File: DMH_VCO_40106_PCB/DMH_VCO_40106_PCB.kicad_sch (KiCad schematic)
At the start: 0 parts

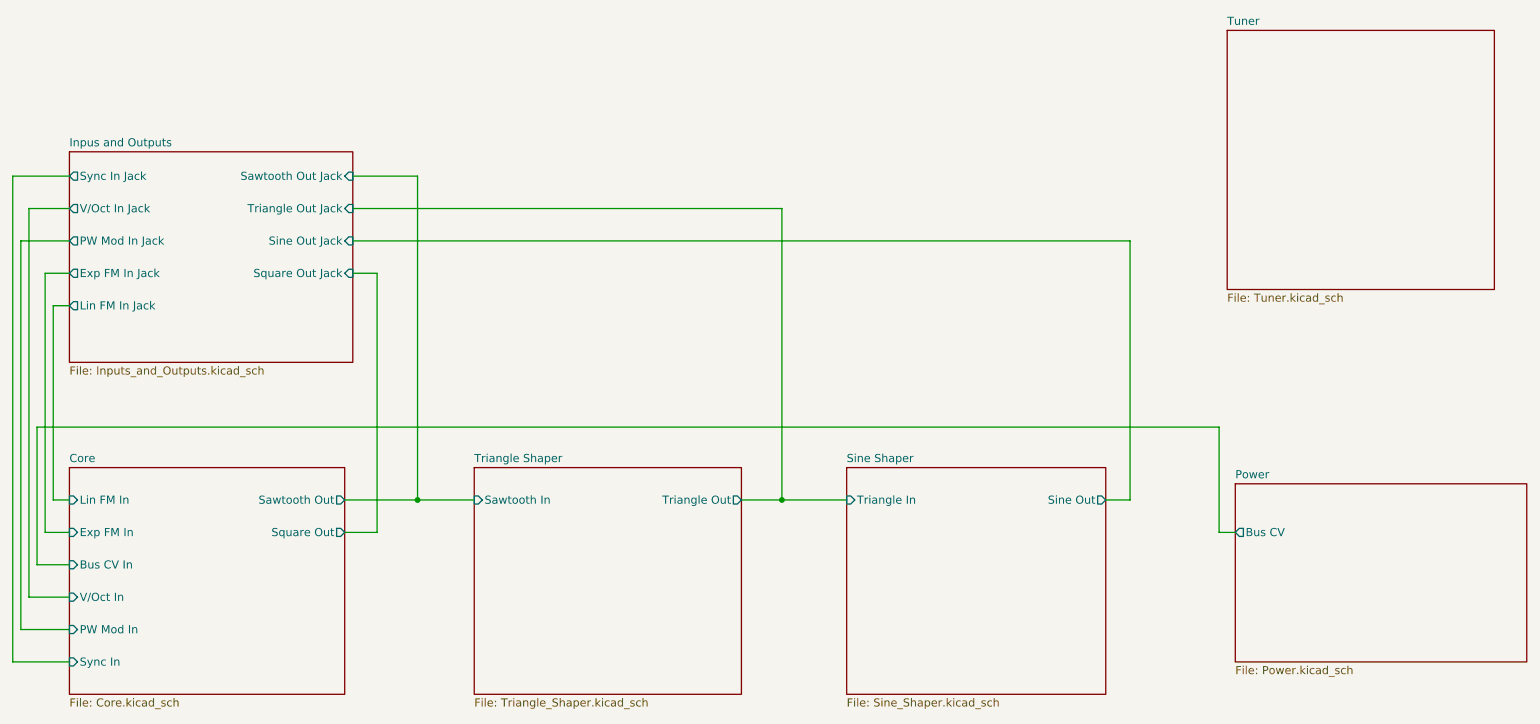
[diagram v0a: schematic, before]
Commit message: Updates from testing on breadboard
- Removed Bus CV input, normalled it to V/oct input jack instead
- Renamed Lin FM input to Exp FM In 2
- Added annotations about temporary resistor/pot values
- Added annotations about pots and trimpots pinout
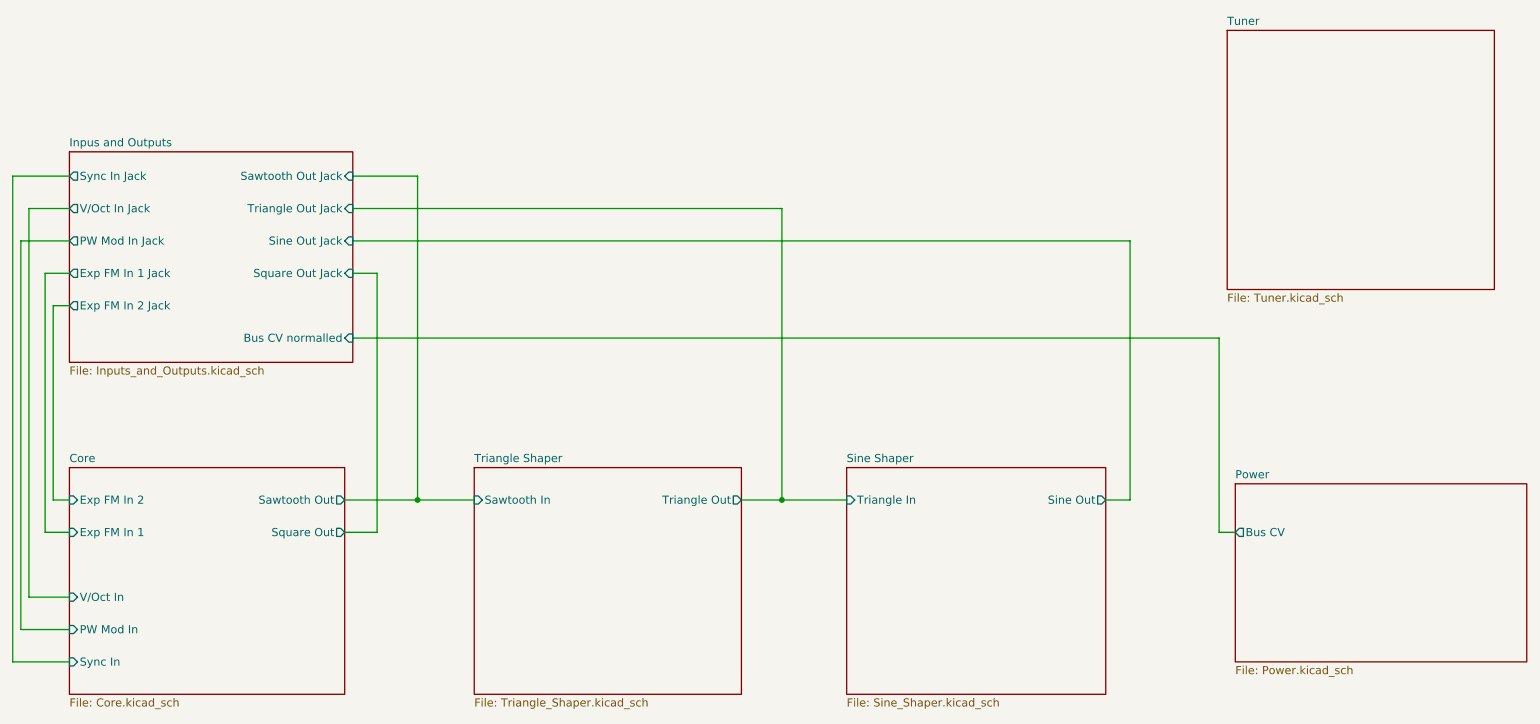
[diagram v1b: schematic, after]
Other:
- sheet Core ports: added Exp FM In 1, Exp FM In 2; removed Bus CV In, Exp FM In, Lin FM In
- sheet Inpus and Outputs ports: added Bus CV normalled, Exp FM In 1 Jack, Exp FM In 2 Jack; removed Exp FM In Jack, Lin FM In Jack
- company: DMH -> DMH Instruments
- title: VCO mki PCB -> VCO 40106 PCB
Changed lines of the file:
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@@
 	(paper "A4")
 	(title_block
-		(title "VCO mki PCB")
+		(title "VCO 40106 PCB")
 		(date "2024-06-16")
 		(rev "1")
-		(company "DMH")
+		(company "DMH Instruments")
 	)
 	(junction
@@
 	(wire
 		(pts
-			(xy 22.86 114.3) (xy 22.86 92.71)
-		)
-		(stroke
-			(width 0)
-			(type default)
-		)
-	)
-	(wire
-		(pts
 			(xy 20.32 63.5) (xy 27.94 63.5)
 		)
@@
 	(wire
 		(pts
-			(xy 208.28 92.71) (xy 208.28 109.22)
-		)
-		(stroke
-			(width 0)
-			(type default)
-		)
-	)
-	(wire
-		(pts
 			(xy 27.94 124.46) (xy 20.32 124.46)
 		)
@@
 	(wire
 		(pts
+			(xy 208.28 78.74) (xy 208.28 109.22)
+		)
+		(stroke
+			(width 0)
+			(type default)
+		)
+	)
+	(wire
+		(pts
 			(xy 19.05 129.54) (xy 27.94 129.54)
 		)
@@
 	(wire
 		(pts
-			(xy 22.86 92.71) (xy 208.28 92.71)
-		)
-		(stroke
-			(width 0)
-			(type default)
-		)
-	)
-	(wire
-		(pts
 			(xy 27.94 68.58) (xy 24.13 68.58)
 		)
@@
 	(wire
 		(pts
+			(xy 208.28 78.74) (xy 72.39 78.74)
+		)
+		(stroke
+			(width 0)
+			(type default)
+		)
+	)
+	(wire
+		(pts
 			(xy 24.13 68.58) (xy 24.13 109.22)
 		)
@@
 		(pts
 			(xy 27.94 119.38) (xy 21.59 119.38)
-		)
-		(stroke
-			(width 0)
-			(type default)
-		)
-	)
-	(wire
-		(pts
-			(xy 27.94 114.3) (xy 22.86 114.3)
 		)
 		(stroke
@@
 			)
 		)
-		(pin "Lin FM In" input
+		(pin "Exp FM In 2" input
 			(at 27.94 104.14 180)
 			(effects
@@
 			)
 		)
-		(pin "Exp FM In" input
+		(pin "Exp FM In 1" input
 			(at 27.94 109.22 180)
-			(effects
-				(font
-					(size 1.27 1.27)
-				)
-				(justify left)
-			)
-		)
-		(pin "Bus CV In" input
-			(at 27.94 114.3 180)
 			(effects
 				(font
@@
 			)
 		)
-		(pin "Exp FM In Jack" output
+		(pin "Exp FM In 1 Jack" output
 			(at 27.94 68.58 180)
 			(effects
@@
 			)
 		)
-		(pin "Lin FM In Jack" output
+		(pin "Exp FM In 2 Jack" output
 			(at 27.94 73.66 180)
 			(effects
@@
 			(effects
 				(font
+					(size 1.27 1.27)
+				)
+				(justify right)
+			)
+		)
+		(pin "Bus CV normalled" input
+			(at 72.39 78.74 0)
+			(effects
+				(font

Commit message: Adjusted all output gains to 10Vpp
... and added buffer stages for Sawtooth Out and Triangle Out in order to avoid modifying Triangle and Sine wafeform characteristics when connecting Sawtooth Out and Triangle Out to other modules.
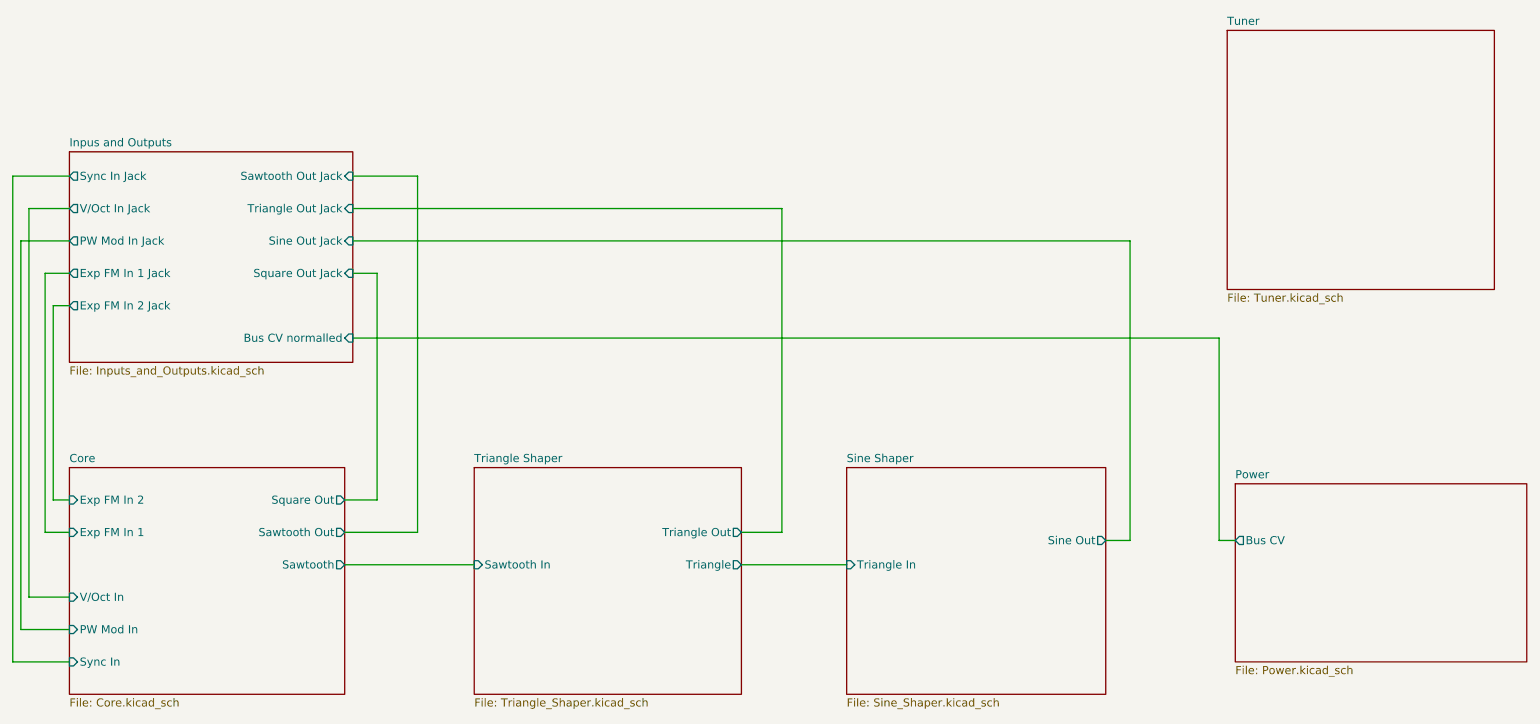
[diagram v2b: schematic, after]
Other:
- sheet Core ports: added Sawtooth; removed none
- sheet Triangle Shaper ports: added Triangle; removed none
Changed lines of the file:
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@@
 		(company "DMH Instruments")
 	)
-	(junction
-		(at 139.7 104.14)
-		(diameter 0)
-		(color 0 0 0 0)
-	)
-	(junction
-		(at 82.55 104.14)
-		(diameter 0)
-		(color 0 0 0 0)
-	)
 	(wire
 		(pts
@@
 	(wire
 		(pts
-			(xy 208.28 109.22) (xy 210.82 109.22)
-		)
-		(stroke
-			(width 0)
-			(type default)
-		)
-	)
-	(wire
-		(pts
-			(xy 194.31 104.14) (xy 194.31 63.5)
+			(xy 208.28 110.49) (xy 210.82 110.49)
+		)
+		(stroke
+			(width 0)
+			(type default)
+		)
+	)
+	(wire
+		(pts
+			(xy 194.31 110.49) (xy 194.31 63.5)
 		)
 		(stroke
@@
 	(wire
 		(pts
-			(xy 71.12 109.22) (xy 76.2 109.22)
-		)
-		(stroke
-			(width 0)
-			(type default)
-		)
-	)
-	(wire
-		(pts
-			(xy 139.7 58.42) (xy 139.7 104.14)
-		)
-		(stroke
-			(width 0)
-			(type default)
-		)
-	)
-	(wire
-		(pts
-			(xy 139.7 104.14) (xy 133.35 104.14)
-		)
-		(stroke
-			(width 0)
-			(type default)
-		)
-	)
-	(wire
-		(pts
-			(xy 208.28 78.74) (xy 208.28 109.22)
+			(xy 71.12 104.14) (xy 76.2 104.14)
+		)
+		(stroke
+			(width 0)
+			(type default)
+		)
+	)
+	(wire
+		(pts
+			(xy 139.7 109.22) (xy 133.35 109.22)
+		)
+		(stroke
+			(width 0)
+			(type default)
+		)
+	)
+	(wire
+		(pts
+			(xy 208.28 78.74) (xy 208.28 110.49)
 		)
 		(stroke
@@
 	(wire
 		(pts
-			(xy 71.12 104.14) (xy 82.55 104.14)
+			(xy 71.12 109.22) (xy 82.55 109.22)
 		)
 		(stroke
@@
 	(wire
 		(pts
-			(xy 139.7 104.14) (xy 149.86 104.14)
-		)
-		(stroke
-			(width 0)
-			(type default)
-		)
-	)
-	(wire
-		(pts
-			(xy 82.55 104.14) (xy 91.44 104.14)
-		)
-		(stroke
-			(width 0)
-			(type default)
-		)
-	)
-	(wire
-		(pts
 			(xy 82.55 53.34) (xy 72.39 53.34)
 		)
@@
 	(wire
 		(pts
+			(xy 71.12 114.3) (xy 91.44 114.3)
+		)
+		(stroke
+			(width 0)
+			(type default)
+		)
+	)
+	(wire
+		(pts
 			(xy 24.13 68.58) (xy 24.13 109.22)
 		)
@@
 	(wire
 		(pts
-			(xy 76.2 109.22) (xy 76.2 68.58)
-		)
-		(stroke
-			(width 0)
-			(type default)
-		)
-	)
-	(wire
-		(pts
-			(xy 82.55 104.14) (xy 82.55 53.34)
+			(xy 76.2 104.14) (xy 76.2 68.58)
+		)
+		(stroke
+			(width 0)
+			(type default)
+		)
+	)
+	(wire
+		(pts
+			(xy 139.7 58.42) (xy 139.7 109.22)
+		)
+		(stroke
+			(width 0)
+			(type default)
+		)
+	)
+	(wire
+		(pts
+			(xy 82.55 109.22) (xy 82.55 53.34)
 		)
 		(stroke
@@
 	(wire
 		(pts
-			(xy 190.5 104.14) (xy 194.31 104.14)
+			(xy 133.35 114.3) (xy 149.86 114.3)
+		)
+		(stroke
+			(width 0)
+			(type default)
+		)
+	)
+	(wire
+		(pts
+			(xy 190.5 110.49) (xy 194.31 110.49)
 		)
 		(stroke
@@
 		)
 		(pin "Triangle Out" output
-			(at 133.35 104.14 0)
+			(at 133.35 109.22 0)
 			(effects
 				(font
@@
 		)
 		(pin "Sawtooth In" input
-			(at 91.44 104.14 180)
-			(effects
-				(font
-					(size 1.27 1.27)
-				)
-				(justify left)
+			(at 91.44 114.3 180)
+			(effects
+				(font
+					(size 1.27 1.27)
+				)
+				(justify left)
+			)
+		)
+		(pin "Triangle" output
+			(at 133.35 114.3 0)
+			(effects
+				(font
+					(size 1.27 1.27)
+				)
+				(justify right)
 			)
 		)
@@
 		)
 		(pin "Sine Out" output
-			(at 190.5 104.14 0)
+			(at 190.5 110.49 0)
 			(effects
 				(font
@@
 		)
 		(pin "Triangle In" input
-			(at 149.86 104.14 180)
+			(at 149.86 114.3 180)
 			(effects
 				(font
@@
 		)
 		(pin "Sawtooth Out" output
+			(at 71.12 109.22 0)
+			(effects
+				(font
+					(size 1.27 1.27)
+				)
+				(justify right)
+			)
+		)
+		(pin "Square Out" output
 			(at 71.12 104.14 0)
-			(effects
-				(font
-					(size 1.27 1.27)
-				)
-				(justify right)
-			)
-		)
-		(pin "Square Out" output
-			(at 71.12 109.22 0)
 			(effects
 				(font
@@
 				)
 				(justify left)
+			)
+		)
+		(pin "Sawtooth" output
+			(at 71.12 114.3 0)
+			(effects
+				(font
+					(size 1.27 1.27)
+				)
+				(justify right)
 			)
 		)
@@
 		)
 		(pin "Bus CV" output
-			(at 210.82 109.22 180)
-			(effects
-				(font
+			(at 210.82 110.49 180)
+			(effects
+				(font

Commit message: Added tuner circuit
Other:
- sheet Tuner ports: added Sawtooth In; removed none
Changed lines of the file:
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@@
 		(company "DMH Instruments")
 	)
+	(junction
+		(at 86.36 114.3)
+		(diameter 0)
+		(color 0 0 0 0)
+	)
 	(wire
 		(pts
@@
 	(wire
 		(pts
+			(xy 209.55 53.34) (xy 86.36 53.34)
+		)
+		(stroke
+			(width 0)
+			(type default)
+		)
+	)
+	(wire
+		(pts
 			(xy 139.7 109.22) (xy 133.35 109.22)
 		)
@@
 	(wire
 		(pts
+			(xy 86.36 53.34) (xy 86.36 114.3)
+		)
+		(stroke
+			(width 0)
+			(type default)
+		)
+	)
+	(wire
+		(pts
 			(xy 27.94 68.58) (xy 24.13 68.58)
 		)
@@
 	(wire
 		(pts
-			(xy 71.12 109.22) (xy 82.55 109.22)
+			(xy 71.12 109.22) (xy 81.28 109.22)
 		)
 		(stroke
@@
 	(wire
 		(pts
-			(xy 82.55 53.34) (xy 72.39 53.34)
+			(xy 81.28 53.34) (xy 72.39 53.34)
 		)
 		(stroke
@@
 	(wire
 		(pts
-			(xy 71.12 114.3) (xy 91.44 114.3)
+			(xy 71.12 114.3) (xy 86.36 114.3)
 		)
 		(stroke
@@
 	(wire
 		(pts
+			(xy 86.36 114.3) (xy 91.44 114.3)
+		)
+		(stroke
+			(width 0)
+			(type default)
+		)
+	)
+	(wire
+		(pts
 			(xy 76.2 104.14) (xy 76.2 68.58)
 		)
@@
 	(wire
 		(pts
-			(xy 82.55 109.22) (xy 82.55 53.34)
+			(xy 81.28 109.22) (xy 81.28 53.34)
 		)
 		(stroke
@@
 			)
 		)
+		(pin "Sawtooth In" input
+			(at 209.55 53.34 180)
+			(effects
+				(font
+					(size 1.27 1.27)
+				)
+				(justify left)
+			)
+		)

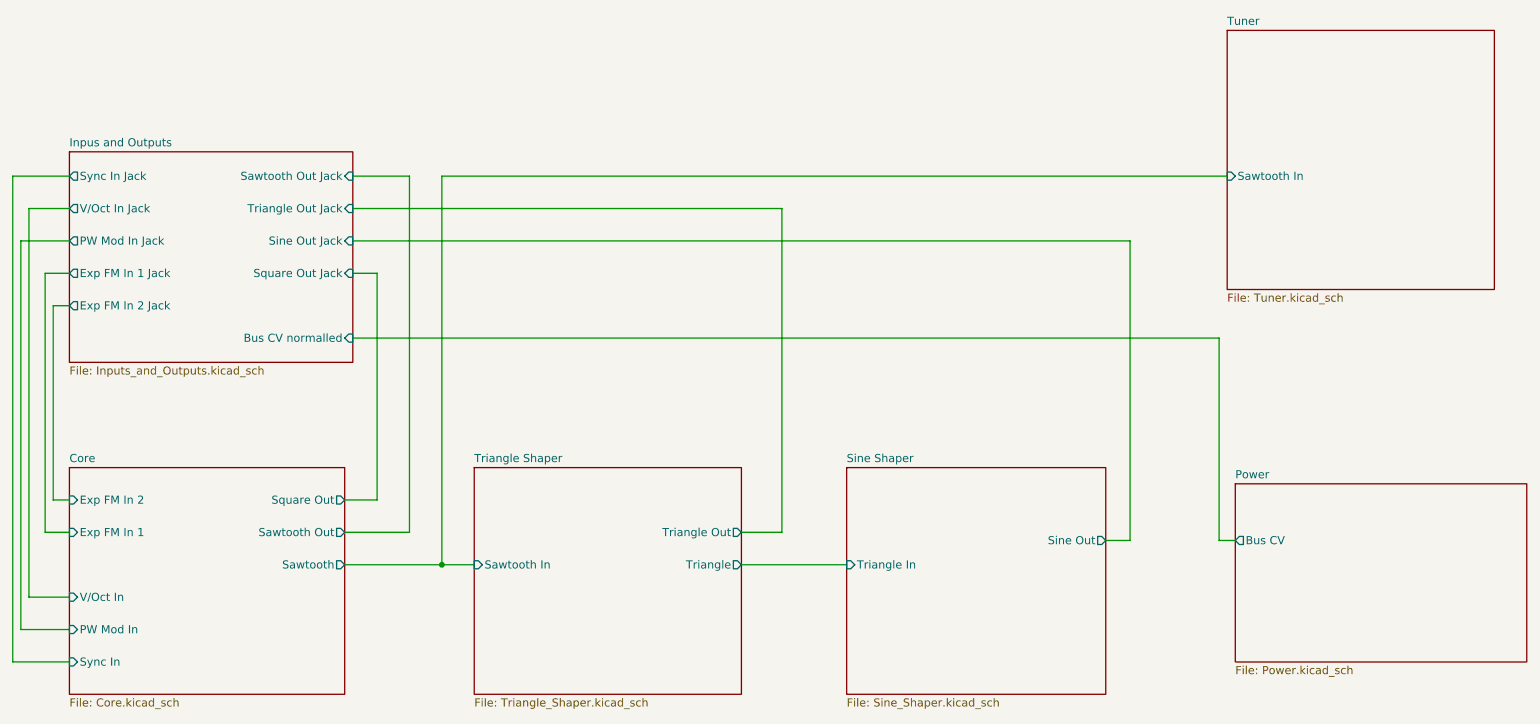
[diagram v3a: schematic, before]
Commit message: Prepared Inputs/Outputs sheet to split in 2 PCBs
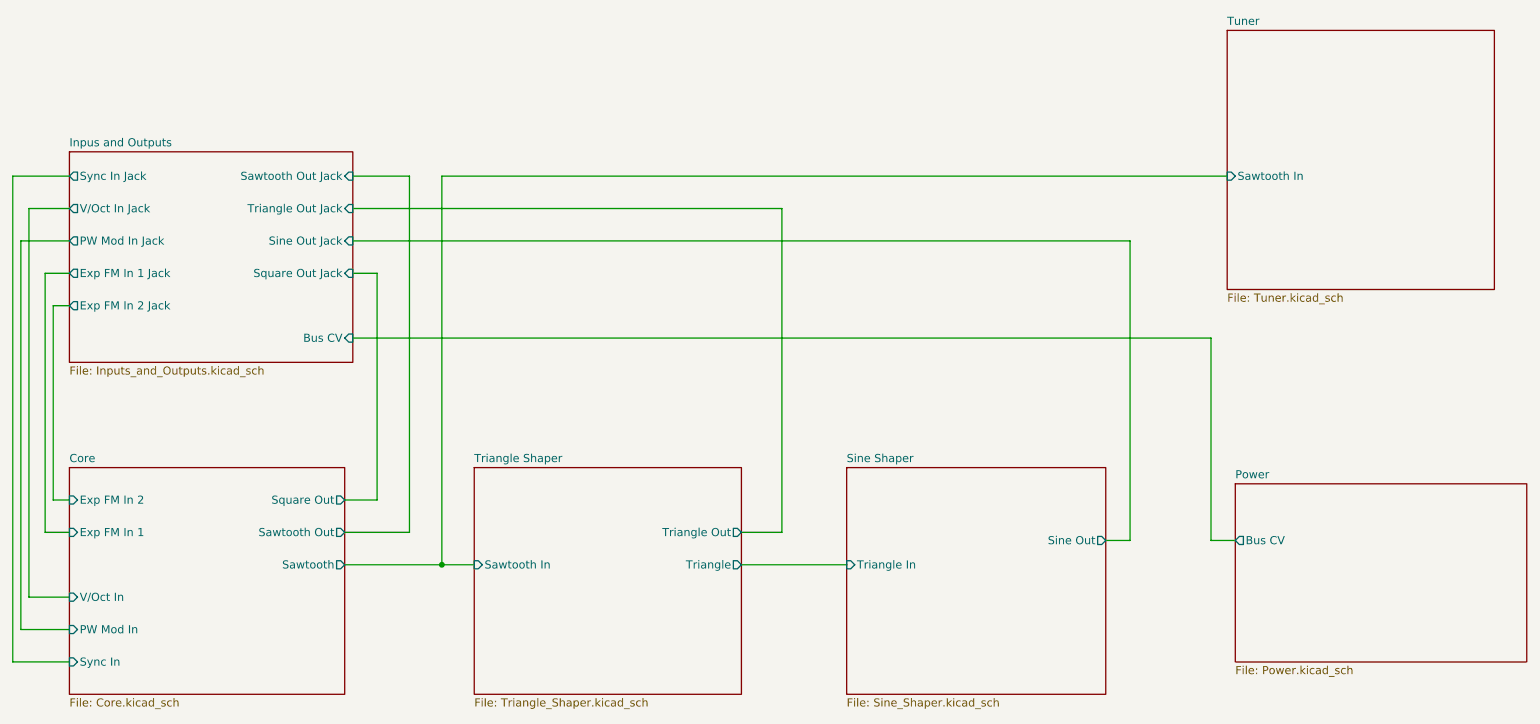
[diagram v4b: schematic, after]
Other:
- sheet Inpus and Outputs ports: added Bus CV; removed Bus CV normalled
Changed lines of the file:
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@@
 	(wire
 		(pts
-			(xy 208.28 110.49) (xy 210.82 110.49)
+			(xy 207.01 110.49) (xy 210.82 110.49)
 		)
 		(stroke
@@
 	(wire
 		(pts
+			(xy 72.39 78.74) (xy 207.01 78.74)
+		)
+		(stroke
+			(width 0)
+			(type default)
+		)
+	)
+	(wire
+		(pts
 			(xy 25.4 73.66) (xy 25.4 104.14)
 		)
@@
 	(wire
 		(pts
-			(xy 208.28 78.74) (xy 208.28 110.49)
+			(xy 207.01 78.74) (xy 207.01 110.49)
 		)
 		(stroke
@@
 		(pts
 			(xy 21.59 119.38) (xy 21.59 58.42)
-		)
-		(stroke
-			(width 0)
-			(type default)
-		)
-	)
-	(wire
-		(pts
-			(xy 208.28 78.74) (xy 72.39 78.74)
 		)
 		(stroke
@@
 			)
 		)
-		(pin "Bus CV normalled" input
+		(pin "Bus CV" input
 			(at 72.39 78.74 0)
 			(effects
